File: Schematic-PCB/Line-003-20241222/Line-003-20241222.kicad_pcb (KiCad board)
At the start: 4 copper layers, 196 x 193.6 mm, 245 parts, among them J1 VIN, J2 Conn_MD, U47 LM393, U48 LM393, U49 LM393, U50 LM393, U51 LM393, U52 LM393, U53 LM393, U54 LM393, U55 LM393, U56 LM393, U57 LM393, U58 LM393, U59 LM393, U60 LM393, U61 LM393, U62 ATmega2560 Pro Board

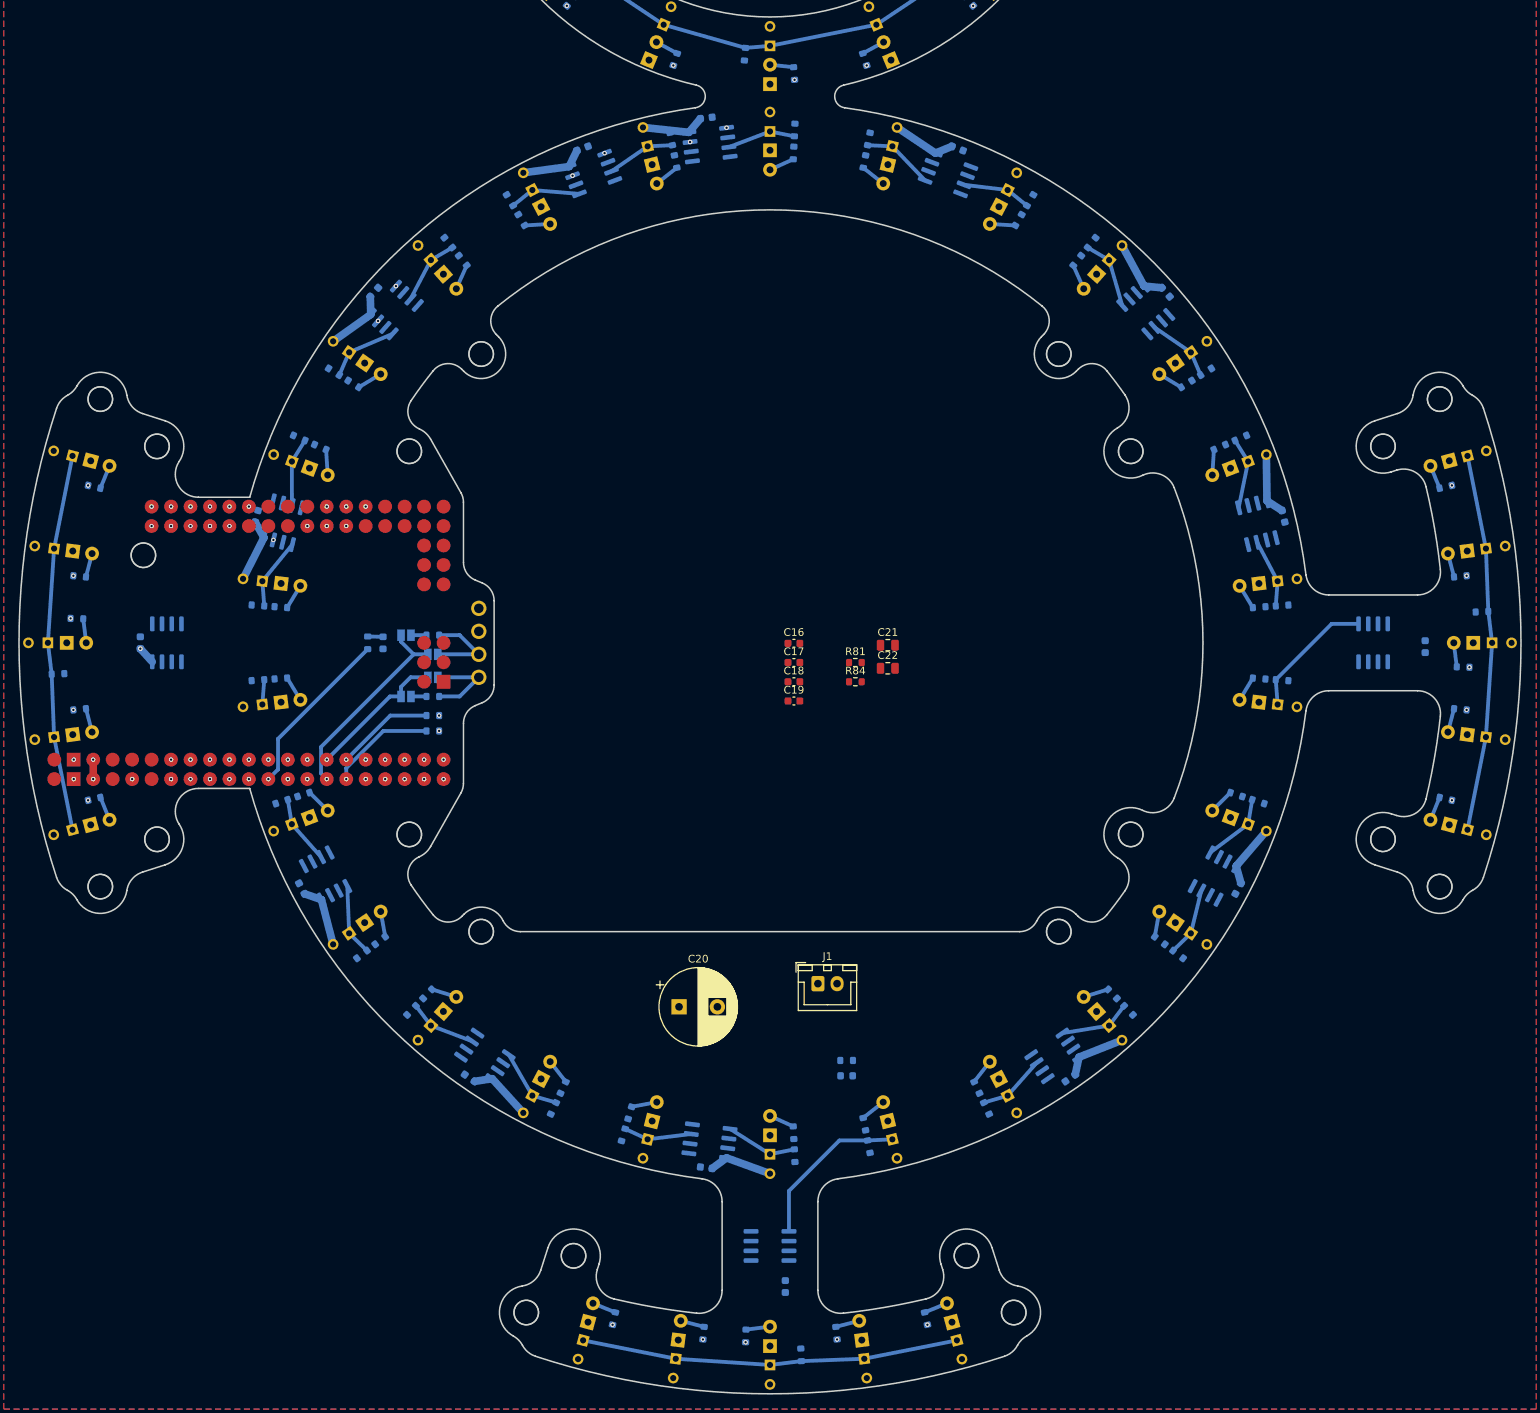
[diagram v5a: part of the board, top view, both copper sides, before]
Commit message: update: 信号線を配線した
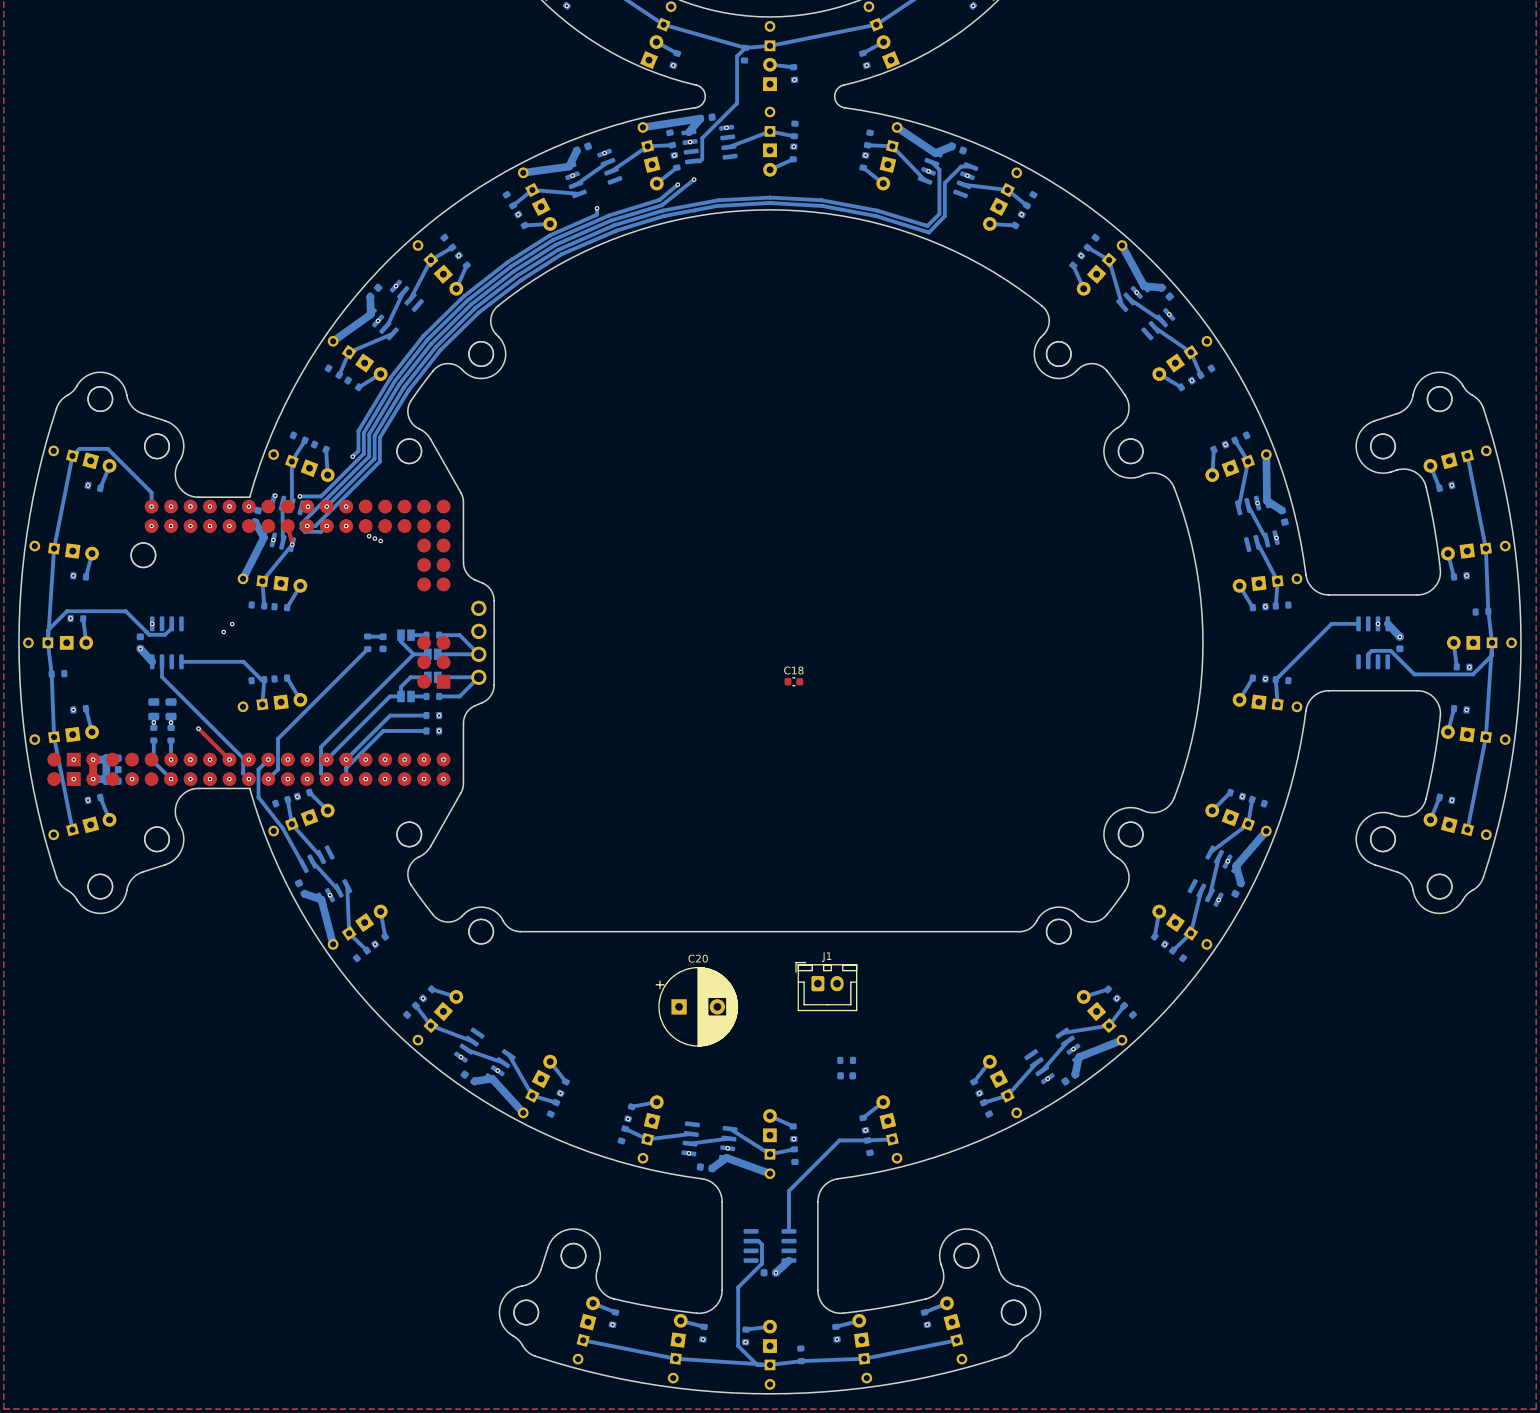
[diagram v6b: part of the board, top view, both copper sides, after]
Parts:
- C16, C17, C19, C21, C22, R81, R84: moved to B.Cu
- moved C22 95.9 mm to (-80.4, 8.68), turned to 90 degrees
- moved C21 93.9 mm to (-78.2, 8.68), turned to 90 degrees
- moved R84 91.8 mm to (-80.4, 11.9), turned to 90 degrees
- moved C16 90.7 mm to (-85.8, 18.1)
- moved C17 90.0 mm to (-85.8, 16.6)
- moved R81 89.8 mm to (-78.2, 11.9), turned to 90 degrees
- moved C19 89.3 mm to (-85.8, 15.1)
- moved C15 3.34 mm to (82.2, -0.00), turned to 90 degrees
- moved C14 2.69 mm to (0.00, 82.2), turned to 0 degrees
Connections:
- U62 pad A0: Line01 -> Line-L
- U62 pad A13: Line-L -> Line01
- U62 pad A15: Line-R -> Line07
- U62 pad A3: Line07 -> Line-R
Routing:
- net 20: track 0.00 -> 218.4 mm, vias 1 -> 2
- net 21: track 0.00 -> 199.0 mm, vias 1 -> 2
- net 22: track 0.00 -> 188.8 mm, vias 1 -> 2
- net 23: track 0.00 -> 173.9 mm, vias 1 -> 2
- net 18: track 0.00 -> 142.6 mm, vias 1 -> 2
- net 19: track 0.00 -> 141.6 mm, vias 1 -> 2
- net 24: track 0.00 -> 132.2 mm, vias 0 -> 2
- net 01: track 0.00 -> 119.0 mm, vias 2 -> 4
- net 16: track 0.00 -> 116.0 mm, vias 1 -> 2
- net 17: track 0.00 -> 114.0 mm, vias 1 -> 2
- net 25: track 0.00 -> 111.3 mm
- net 02: track 0.00 -> 109.9 mm, vias 2 -> 4
- net 26: track 0.00 -> 105.5 mm
- net 03: track 0.00 -> 102.2 mm, vias 2 -> 3
- net 04: track 0.00 -> 80.6 mm, vias 2 -> 3
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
